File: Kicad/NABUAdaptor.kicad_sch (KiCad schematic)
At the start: 102 parts, among them J1 Conn_01x04, J2 DIN-5_180degree, J3 Conn_01x09, J4 Conn_01x05, U1 74LS164, U10 UA9638CD, U11 UA9637, U12 74LS164, U13 74LS164, U14 74LS04, U15 74LS74, U16 N8X60, U17 2114, U18 2114, U19 LM339, U2 74LS30, U20 74LS164, U21 74LS86, U22 74LS74, U23 74LS00, U24 74LS04, U25 74LS00, U26 74LS74, U27 74LS00, U28 74LS74, U29 74LS74, U3 74LS27, U30 74LS02, U31 MC6805P2, U32 74LS74, U33 74HCU04, U4 74LS164, U5 PAL16R6 (ID PAL), U6 74LS374, U7 74LS373, U8 ?VALUE?, U9 TR1865PL, Y1 3.579545MHz

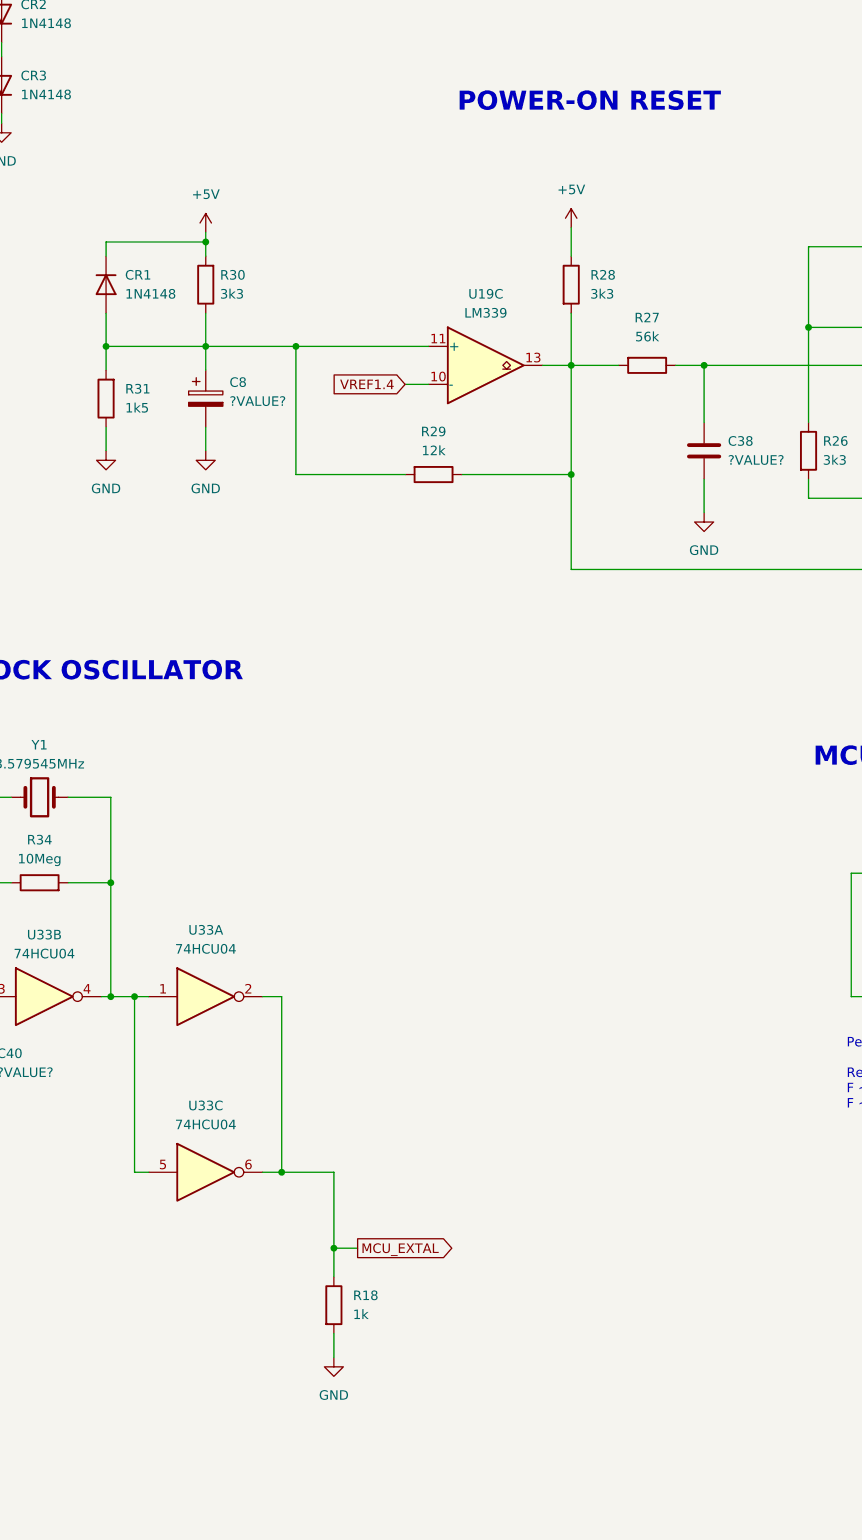
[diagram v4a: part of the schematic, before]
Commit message: tidy around oscs, add reset circuit timing, add LTSpice POR model
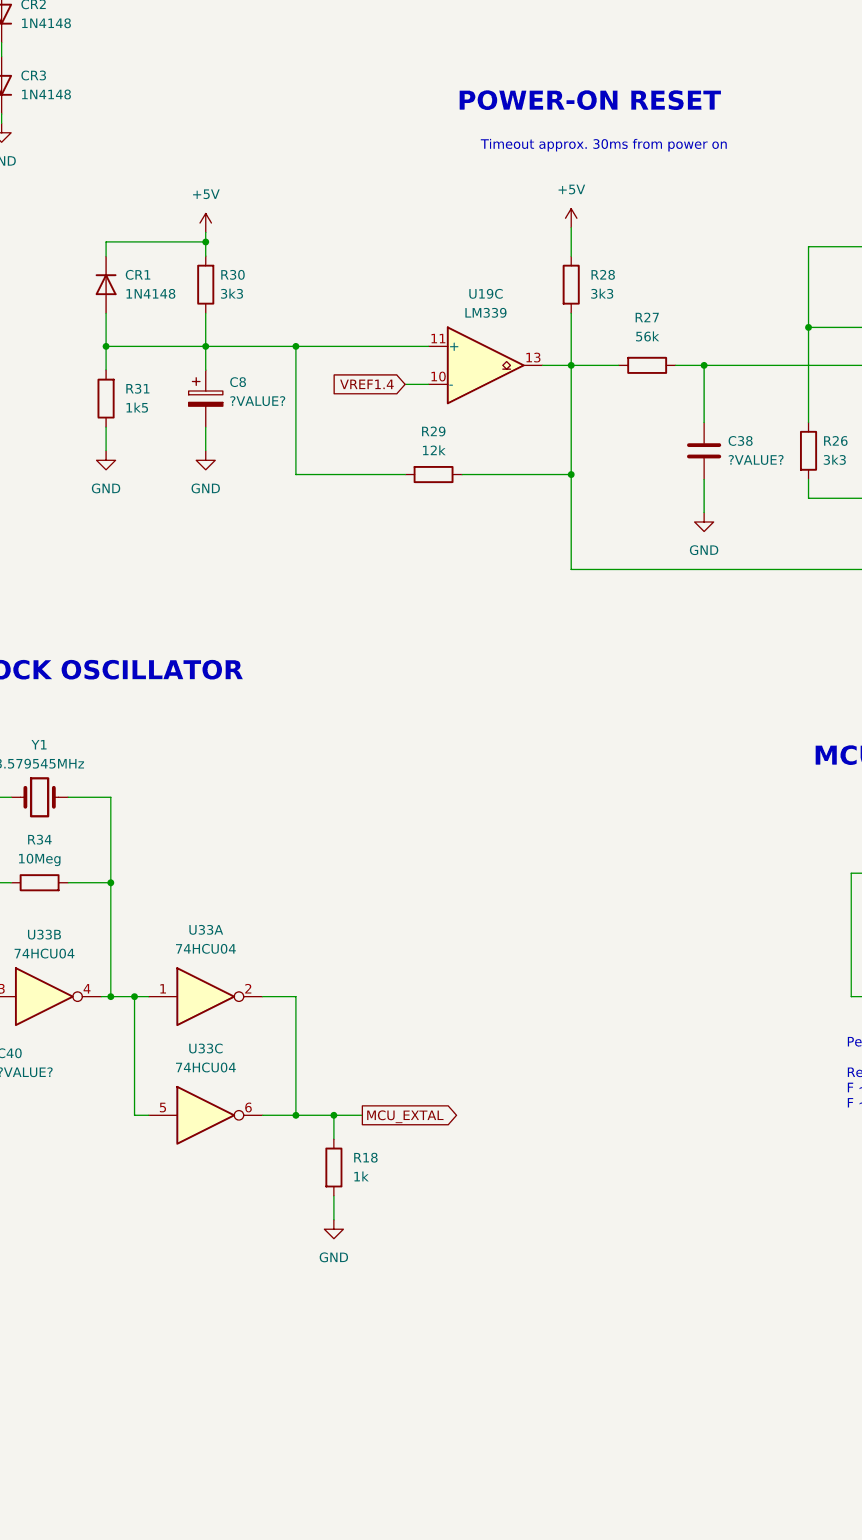
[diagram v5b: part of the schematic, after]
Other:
- note added: "Timeout approx. 30ms from power on"
- moved on the sheet: R18, U33C
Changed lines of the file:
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@@
   (junction (at 411.48 189.23) (diameter 0) (color 0 0 0 0)
   )
-  (junction (at 648.335 317.5) (diameter 0) (color 0 0 0 0)
-  )
   (junction (at 473.075 415.925) (diameter 0) (color 0 0 0 0)
   )
@@
   (junction (at 305.943 527.685) (diameter 0) (color 0 0 0 0)
   )
+  (junction (at 650.24 309.88) (diameter 0) (color 0 0 0 0)
+  )
   (junction (at 746.125 207.01) (diameter 0) (color 0 0 0 0)
   )
@@
   (junction (at 88.9 144.145) (diameter 0) (color 0 0 0 0)
   )
-  (junction (at 655.32 327.66) (diameter 0) (color 0 0 0 0)
-  )
   (junction (at 361.95 163.195) (diameter 0) (color 0 0 0 0)
   )
@@
   (junction (at 778.51 128.905) (diameter 0) (color 0 0 0 0)
   )
+  (junction (at 655.32 309.88) (diameter 0) (color 0 0 0 0)
+  )
   (junction (at 305.943 554.355) (diameter 0) (color 0 0 0 0)
   )
@@
     (stroke (width 0) (type default))
   )
-  (wire (pts (xy 655.32 317.5) (xy 655.32 327.66))
-    (stroke (width 0) (type default))
-  )
   (wire (pts (xy 741.68 277.495) (xy 743.585 277.495))
     (stroke (width 0) (type default))
@@
     (stroke (width 0) (type default))
   )
+  (wire (pts (xy 650.24 309.88) (xy 655.32 309.88))
+    (stroke (width 0) (type default))
+  )
   (bus (pts (xy 569.595 93.98) (xy 583.565 93.98))
     (stroke (width 0) (type default))
@@
     (stroke (width 0) (type default))
   )
-  (wire (pts (xy 648.335 294.005) (xy 648.335 317.5))
+  (wire (pts (xy 650.24 294.005) (xy 650.24 309.88))
     (stroke (width 0) (type default))
   )
@@
     (stroke (width 0) (type default))
   )
-  (wire (pts (xy 648.335 317.5) (xy 645.795 317.5))
+  (wire (pts (xy 645.795 309.88) (xy 650.24 309.88))
     (stroke (width 0) (type default))
   )
@@
     (stroke (width 0) (type default))
   )
+  (wire (pts (xy 655.32 309.88) (xy 655.32 313.055))
+    (stroke (width 0) (type default))
+  )
   (bus (pts (xy 113.03 422.275) (xy 113.03 419.735))
     (stroke (width 0) (type default))
@@
     (stroke (width 0) (type default))
   )
-  (wire (pts (xy 628.65 294.005) (xy 628.65 317.5))
+  (wire (pts (xy 628.65 294.005) (xy 628.65 309.88))
     (stroke (width 0) (type default))
   )
@@
     (stroke (width 0) (type default))
   )
-  (wire (pts (xy 648.335 317.5) (xy 655.32 317.5))
-    (stroke (width 0) (type default))
-  )
   (wire (pts (xy 115.57 419.735) (xy 122.555 419.735))
     (stroke (width 0) (type default))
@@
     (stroke (width 0) (type default))
   )
-  (wire (pts (xy 655.32 327.66) (xy 655.32 331.47))
-    (stroke (width 0) (type default))
-  )
   (wire (pts (xy 170.815 151.13) (xy 175.26 151.13))
     (stroke (width 0) (type default))
@@
     (stroke (width 0) (type default))
   )
+  (wire (pts (xy 645.795 294.005) (xy 650.24 294.005))
+    (stroke (width 0) (type default))
+  )
   (wire (pts (xy 253.365 326.39) (xy 254.635 326.39))
     (stroke (width 0) (type default))
@@
     (stroke (width 0) (type default))
   )
-  (wire (pts (xy 658.495 327.66) (xy 655.32 327.66))
+  (wire (pts (xy 659.13 309.88) (xy 655.32 309.88))
     (stroke (width 0) (type default))
   )
@@
     (stroke (width 0) (type default))
   )
-  (wire (pts (xy 630.555 317.5) (xy 628.65 317.5))
+  (wire (pts (xy 630.555 309.88) (xy 628.65 309.88))
     (stroke (width 0) (type default))
   )
@@
     (stroke (width 0) (type default))
   )
-  (wire (pts (xy 645.795 294.005) (xy 648.335 294.005))
-    (stroke (width 0) (type default))
-  )
   (bus (pts (xy 161.925 409.575) (xy 161.925 407.035))
     (stroke (width 0) (type default))
@@
     (stroke (width 0) (type default))
   )
-  (wire (pts (xy 655.32 339.09) (xy 655.32 342.265))
+  (wire (pts (xy 655.32 320.675) (xy 655.32 323.85))
     (stroke (width 0) (type default))
   )
@@
     (effects (font (size 2.54 2.54) (thickness 0.508) bold) (justify left bottom))
   )
+  (text "Timeout approx. 30ms from power on" (at 708.025 180.975 0)
+    (effects (font (size 1.27 1.27)) (justify right bottom))
+  )
   (text "MCU TIMER REFERENCE OSCILLATOR" (at 719.455 263.525 0)
     (effects (font (size 2.54 2.54) (thickness 0.508) bold) (justify left bottom))
@@
     )
   )
-  (global_label "MCU_EXTAL" (shape output) (at 658.495 327.66 0) (fields_autoplaced)
+  (global_label "MCU_EXTAL" (shape output) (at 659.13 309.88 0) (fields_autoplaced)
     (effects (font (size 1.27 1.27)) (justify left))
-    (property "Intersheetrefs" "${INTERSHEET_REFS}" (at 671.9425 327.66 0)
+    (property "Intersheetrefs" "${INTERSHEET_REFS}" (at 672.5775 309.88 0)
       (effects (font (size 1.27 1.27)) (justify left))
     )
@@
     )
   )
-  (symbol (lib_id "74xx:74HC04") (at 638.175 317.5 0) (unit 3)
+  (symbol (lib_id "74xx:74HC04") (at 638.175 309.88 0) (unit 3)
     (in_bom yes) (on_board yes) (dnp no) (fields_autoplaced)
-    (property "Reference" "U33" (at 638.175 308.61 0)
+    (property "Reference" "U33" (at 638.175 300.99 0)
       (effects (font (size 1.27 1.27)))
     )
-    (property "Value" "74HCU04" (at 638.175 311.15 0)
+    (property "Value" "74HCU04" (at 638.175 303.53 0)
       (effects (font (size 1.27 1.27)))
     )
-    (property "Footprint" "" (at 638.175 317.5 0)
+    (property "Footprint" "" (at 638.175 309.88 0)
       (effects (font (size 1.27 1.27)) hide)
     )
-    (property "Datasheet" "https://assets.nexperia.com/documents/data-sheet/74HC_HCT04.pdf" (at 638.175 317.5 0)
+    (property "Datasheet" "https://assets.nexperia.com/documents/data-sheet/74HC_HCT04.pdf" (at 638.175 309.88 0)
       (effects (font (size 1.27 1.27)) hide)
     )
@@
     )
   )
-  (symbol (lib_id "power:GND") (at 655.32 342.265 0) (unit 1)
+  (symbol (lib_id "power:GND") (at 655.32 323.85 0) (unit 1)
     (in_bom yes) (on_board yes) (dnp no) (fields_autoplaced)
-    (property "Reference" "#PWR079" (at 655.32 348.615 0)
+    (property "Reference" "#PWR079" (at 655.32 330.2 0)
       (effects (font (size 1.27 1.27)) hide)
     )
-    (property "Value" "GND" (at 655.32 347.345 0)
+    (property "Value" "GND" (at 655.32 328.93 0)
       (effects (font (size 1.27 1.27)))
     )
-    (property "Footprint" "" (at 655.32 342.265 0)
+    (property "Footprint" "" (at 655.32 323.85 0)
       (effects (font (size 1.27 1.27)) hide)
     )
-    (property "Datasheet" "" (at 655.32 342.265 0)
+    (property "Datasheet" "" (at 655.32 323.85 0)
       (effects (font (size 1.27 1.27)) hide)
     )
@@
     )
   )
-  (symbol (lib_id "Device:R") (at 655.32 335.28 0) (unit 1)
+  (symbol (lib_id "Device:R") (at 655.32 316.865 0) (unit 1)
     (in_bom yes) (on_board yes) (dnp no) (fields_autoplaced)
-    (property "Reference" "R18" (at 657.86 334.01 0)
+    (property "Reference" "R18" (at 657.86 315.595 0)
       (effects (font (size 1.27 1.27)) (justify left))
     )
-    (property "Value" "1k" (at 657.86 336.55 0)
+    (property "Value" "1k" (at 657.86 318.135 0)
       (effects (font (size 1.27 1.27)) (justify left))
     )
-    (property "Footprint" "" (at 653.542 335.28 90)
+    (property "Footprint" "" (at 653.542 316.865 90)
       (effects (font (size 1.27 1.27)) hide)
     )
-    (property "Datasheet" "~" (at 655.32 335.28 0)
+    (property "Datasheet" "~" (at 655.32 316.865 0)
       (effects (font (size 1.27 1.27)) hide)
     )

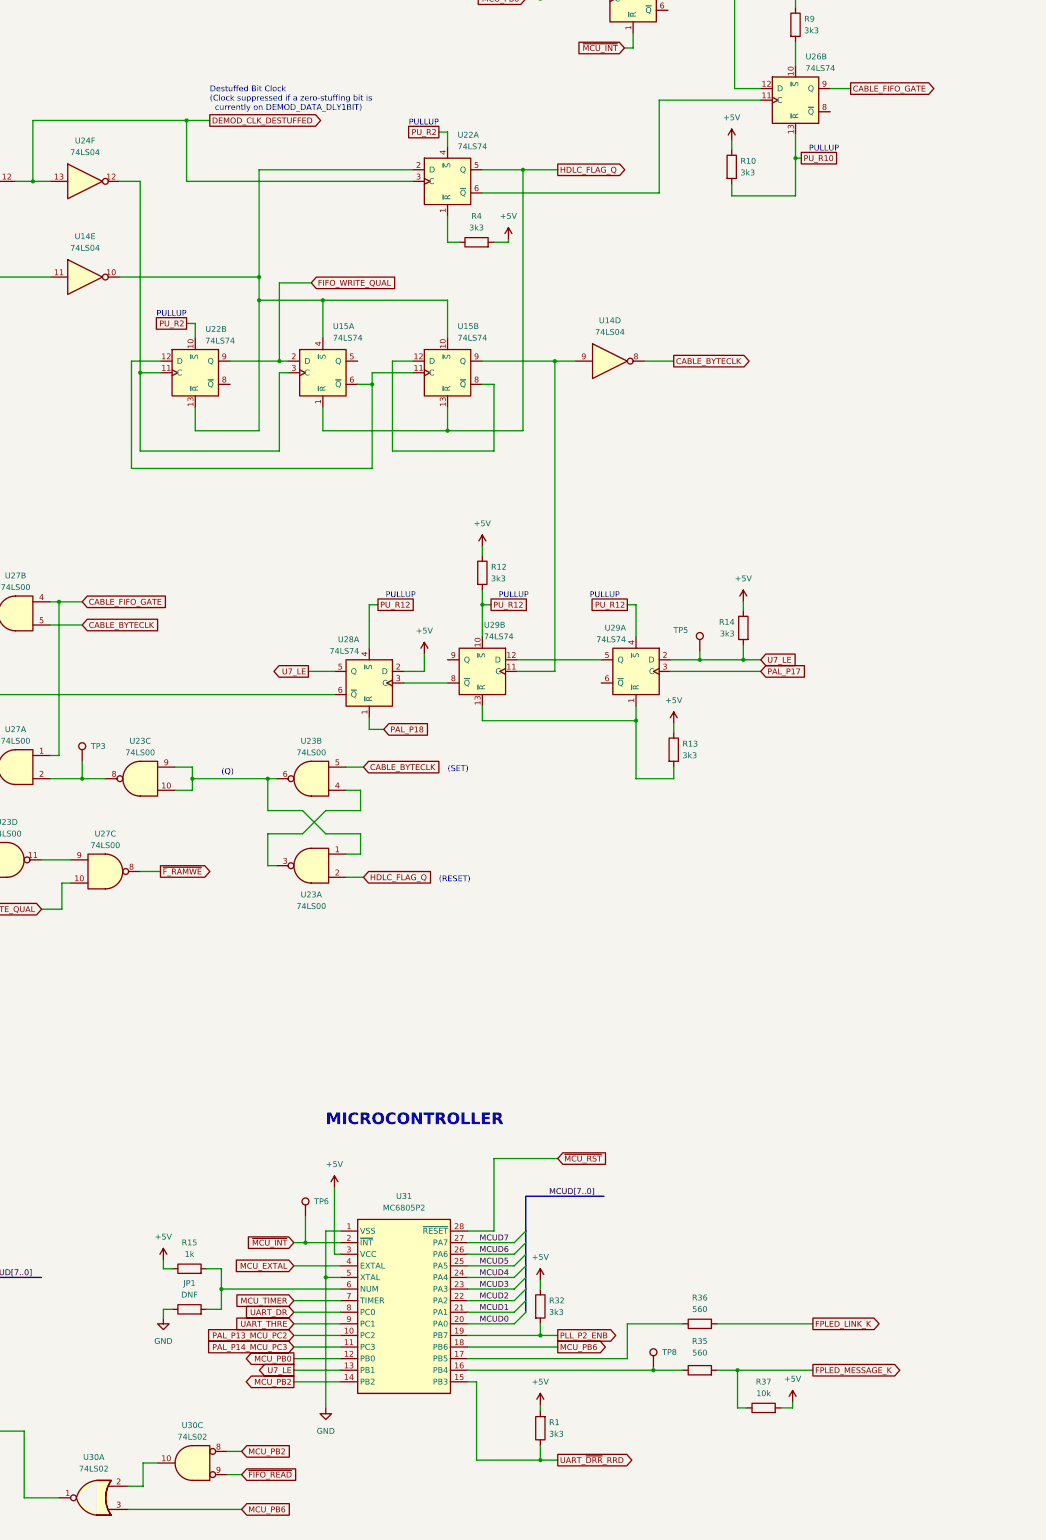
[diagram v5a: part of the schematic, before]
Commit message: Add more pin descriptions
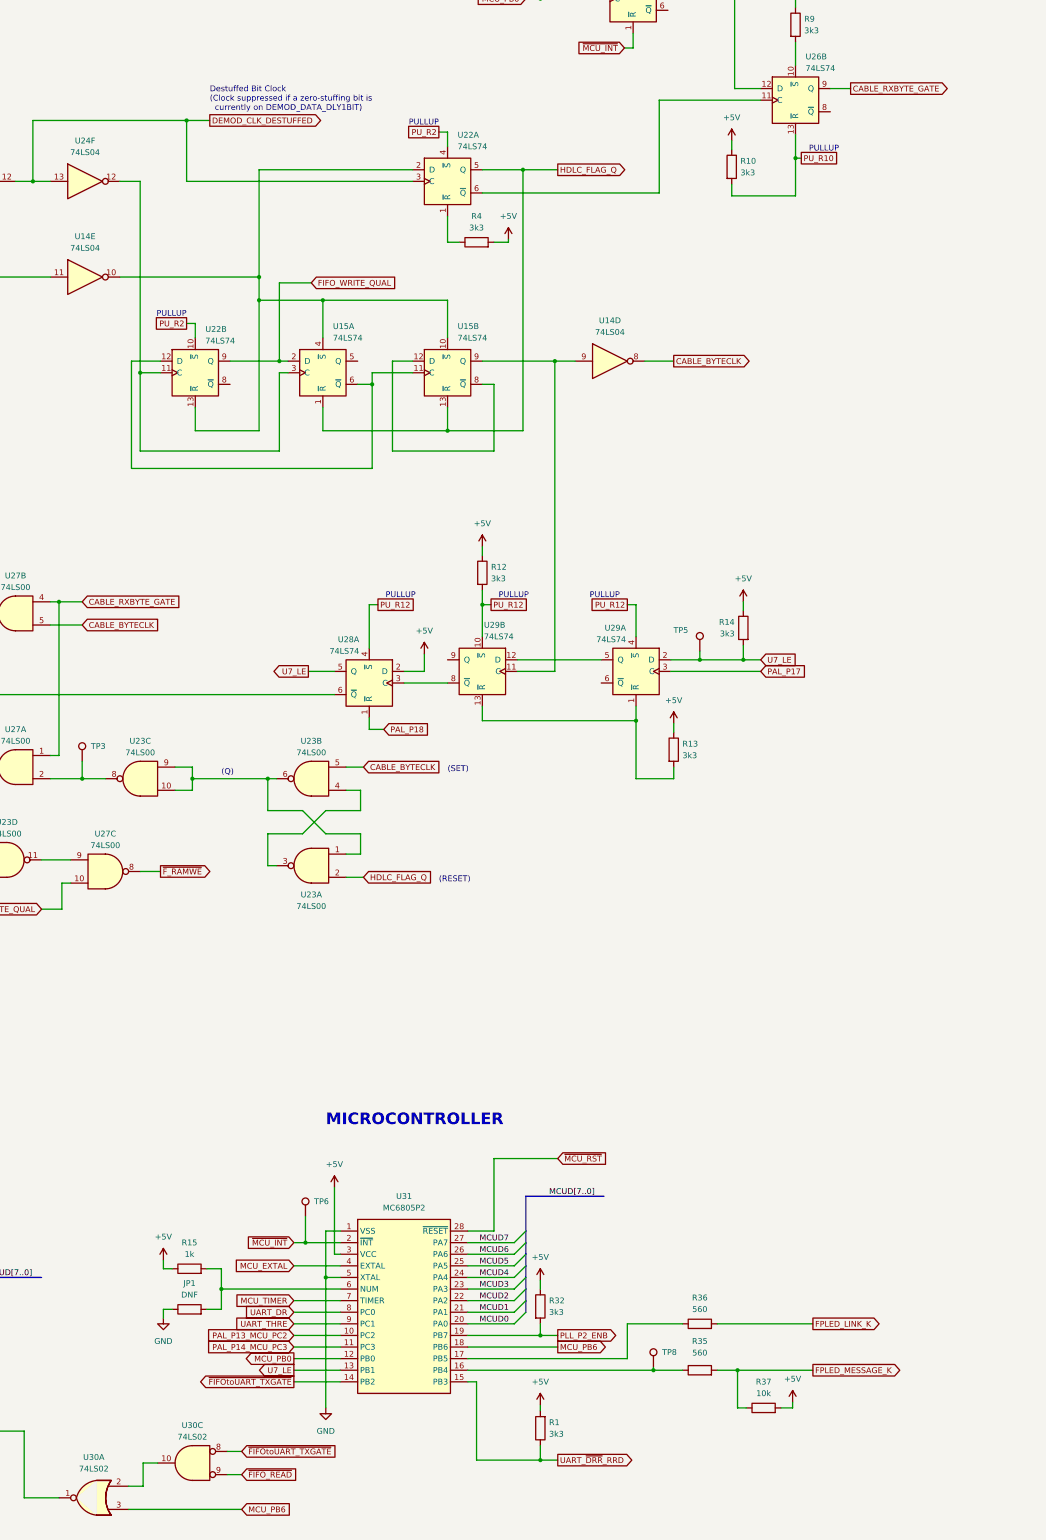
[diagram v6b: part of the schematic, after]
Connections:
- net CABLE_FIFO_GATE renamed CABLE_RXBYTE_GATE
- net MCU_PB2 renamed ~{FIFOtoUART_TXGATE}
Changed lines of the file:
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@@
     )
   )
-  (global_label "MCU_PB2" (shape output) (at 419.1 426.085 180) (fields_autoplaced)
+  (global_label "~{FIFOtoUART_TXGATE}" (shape output) (at 419.1 426.085 180) (fields_autoplaced)
     (effects (font (size 1.27 1.27)) (justify right))
     (property "Intersheetrefs" "${INTERSHEET_REFS}" (at 407.3458 426.085 0)
@@
     )
   )
-  (global_label "MCU_PB2" (shape input) (at 407.67 441.325 0) (fields_autoplaced)
+  (global_label "~{FIFOtoUART_TXGATE}" (shape input) (at 407.67 441.325 0) (fields_autoplaced)
     (effects (font (size 1.27 1.27)) (justify left))
     (property "Intersheetrefs" "${INTERSHEET_REFS}" (at 419.4242 441.325 0)
@@
     )
   )
-  (global_label "CABLE_FIFO_GATE" (shape output) (at 541.02 142.875 0) (fields_autoplaced)
+  (global_label "CABLE_RXBYTE_GATE" (shape output) (at 541.02 142.875 0) (fields_autoplaced)
     (effects (font (size 1.27 1.27)) (justify left))
     (property "Intersheetrefs" "${INTERSHEET_REFS}" (at 560.3338 142.875 0)
@@
     )
   )
-  (global_label "CABLE_FIFO_GATE" (shape input) (at 372.745 255.27 0) (fields_autoplaced)
+  (global_label "CABLE_RXBYTE_GATE" (shape input) (at 372.745 255.27 0) (fields_autoplaced)
     (effects (font (size 1.27 1.27)) (justify left))
     (property "Intersheetrefs" "${INTERSHEET_REFS}" (at 392.0588 255.27 0)
